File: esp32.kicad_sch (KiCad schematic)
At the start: 17 parts, among them J5 UART, J6 ToSSR, J7 USB_A, Q1 BSS138, SW1 SW_Push, SW2 SW_Push, U1 ESP32-S3-WROOM-1

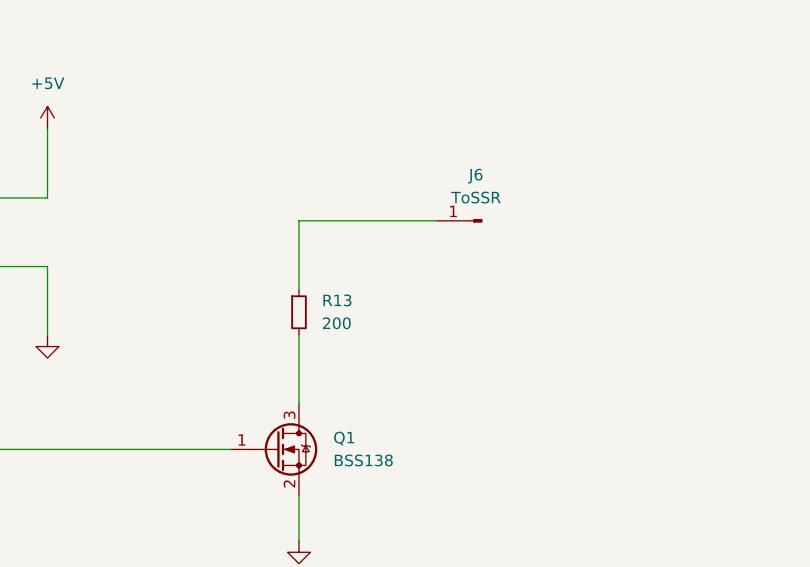
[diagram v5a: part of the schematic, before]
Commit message: fix: add connector JST to SSR device
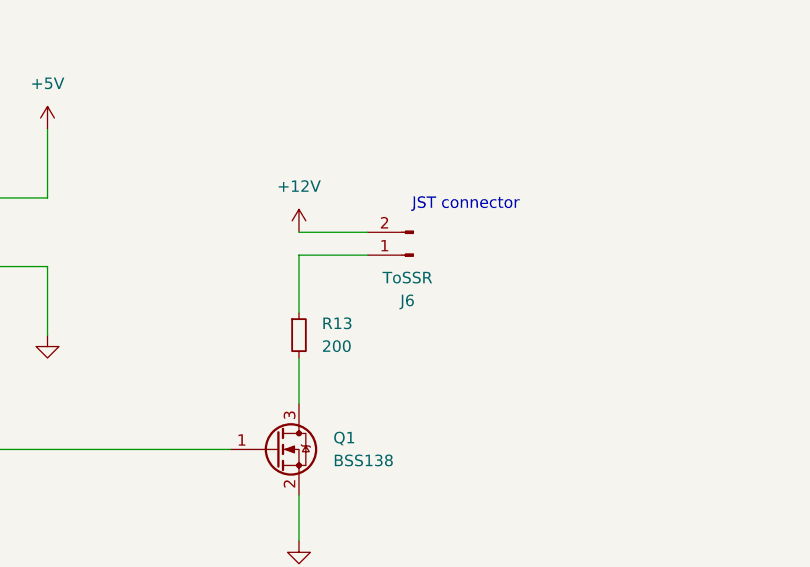
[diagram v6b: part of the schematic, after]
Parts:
- removed J6: ToSSR, Connector_PinHeader_2.54mm:PinHeader_1x01_P2.54mm_Vertical, symbol Connector:Conn_01x01_Pin
- added J6: ToSSR, symbol Connector:Conn_01x02_Pin
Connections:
- net at R13.1: now also J6.1 (Pin_1)
- new net +12V: J6.2 (Pin_2)
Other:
- note added: "JST connector"
- moved on the sheet: R13
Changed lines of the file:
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@@
 	(generator_version "9.0")
 	(paper "A4")
+	(text "JST connector"
+		(exclude_from_sim no)
+		(at 188.722 64.262 0)
+		(effects
+			(font
+				(size 1.27 1.27)
+			)
+		)
+	)
 	(junction
 		(at 92.71 44.45)
@@
 	(wire
 		(pts
-			(xy 170.18 78.74) (xy 170.18 86.36)
+			(xy 170.18 81.28) (xy 170.18 86.36)
 		)
 		(stroke
@@
 	(wire
 		(pts
-			(xy 170.18 66.04) (xy 170.18 73.66)
+			(xy 170.18 69.85) (xy 170.18 76.2)
 		)
 		(stroke
@@
 	(wire
 		(pts
+			(xy 170.18 67.31) (xy 177.8 67.31)
+		)
+		(stroke
+			(width 0)
+			(type default)
+		)
+	)
+	(wire
+		(pts
 			(xy 107.95 91.44) (xy 162.56 91.44)
 		)
@@
 	(wire
 		(pts
-			(xy 185.42 66.04) (xy 170.18 66.04)
-		)
-		(stroke
-			(width 0)
-			(type default)
-		)
-	)
-	(wire
-		(pts
 			(xy 142.24 55.88) (xy 142.24 63.5)
+		)
+		(stroke
+			(width 0)
+			(type default)
+		)
+	)
+	(wire
+		(pts
+			(xy 170.18 69.85) (xy 177.8 69.85)
 		)
 		(stroke
@@
 	(symbol
 		(lib_id "Device:R_Small")
-		(at 170.18 76.2 0)
+		(at 170.18 78.74 0)
 		(unit 1)
 		(exclude_from_sim no)
@@
 		(fields_autoplaced yes)
 		(property "Reference" "R13"
-			(at 172.72 74.93 0)
+			(at 172.72 77.47 0)
 			(effects
 				(font
@@
 		)
 		(property "Value" "200"
-			(at 172.72 77.47 0)
+			(at 172.72 80.01 0)
 			(effects
 				(font
@@
 		)
 		(property "Footprint" "Resistor_THT:R_Axial_DIN0207_L6.3mm_D2.5mm_P7.62mm_Horizontal"
-			(at 170.18 76.2 0)
+			(at 170.18 78.74 0)
 			(effects
 				(font
@@
 		)
 		(property "Datasheet" "dispo 180 ou 220"
-			(at 170.18 76.2 0)
+			(at 170.18 78.74 0)
 			(effects
 				(font
@@
 		)
 		(property "Description" ""
-			(at 170.18 76.2 0)
+			(at 170.18 78.74 0)
 			(effects
 				(font
@@
 	)
 	(symbol
-		(lib_id "Connector:Conn_01x01_Pin")
-		(at 190.5 66.04 180)
-		(unit 1)
-		(exclude_from_sim no)
-		(in_bom yes)
-		(on_board yes)
-		(dnp no)
-		(fields_autoplaced yes)
-		(property "Reference" "J6"
-			(at 189.865 60.96 0)
-			(effects
-				(font
-					(size 1.27 1.27)
-				)
-			)
-		)
-		(property "Value" "ToSSR"
-			(at 189.865 63.5 0)
-			(effects
-				(font
-					(size 1.27 1.27)
-				)
-			)
-		)
-		(property "Footprint" "Connector_PinHeader_2.54mm:PinHeader_1x01_P2.54mm_Vertical"
-			(at 190.5 66.04 0)
-			(effects
-				(font
-					(size 1.27 1.27)
-				)
-				(hide yes)
-			)
-		)
-		(property "Datasheet" "~"
-			(at 190.5 66.04 0)
-			(effects
-				(font
-					(size 1.27 1.27)
-				)
-				(hide yes)
-			)
-		)
-		(property "Description" ""
-			(at 190.5 66.04 0)
-			(effects
-				(font
-					(size 1.27 1.27)
-				)
-				(hide yes)
-			)
-		)
-		(pin "1"
-		)
-		(instances
-			(project "pv_router"
-				(path "/08ef31dc-81c2-4bcd-8336-e62c344e451e/5b2a06a5-fb5f-4aba-bfde-32c85173e89f"
-					(reference "J6")
-					(unit 1)
-				)
-			)
-		)
-	)
-	(symbol
 		(lib_id "Device:C")
 		(at 60.96 66.04 90)
@@
 	)
 	(symbol
+		(lib_id "power:+12V")
+		(at 170.18 67.31 0)
+		(unit 1)
+		(exclude_from_sim no)
+		(in_bom yes)
+		(on_board yes)
+		(dnp no)
+		(fields_autoplaced yes)
+		(property "Reference" "#PWR020"
+			(at 170.18 71.12 0)
+			(effects
+				(font
+					(size 1.27 1.27)
+				)
+				(hide yes)
+			)
+		)
+		(property "Value" "+12V"
+			(at 170.18 62.23 0)
+			(effects
+				(font
+					(size 1.27 1.27)
+				)
+			)
+		)
+		(property "Footprint" ""
+			(at 170.18 67.31 0)
+			(effects
+				(font
+					(size 1.27 1.27)
+				)
+				(hide yes)
+			)
+		)
+		(property "Datasheet" ""
+			(at 170.18 67.31 0)
+			(effects
+				(font
+					(size 1.27 1.27)
+				)
+				(hide yes)
+			)
+		)
+		(property "Description" "Power symbol creates a global label with name \"+12V\""
+			(at 170.18 67.31 0)
+			(effects
+				(font
+					(size 1.27 1.27)
+				)
+				(hide yes)
+			)
+		)
+		(pin "1"
+		)
+		(instances
+			(project ""
+				(path "/08ef31dc-81c2-4bcd-8336-e62c344e451e/5b2a06a5-fb5f-4aba-bfde-32c85173e89f"
+					(reference "#PWR020")
+					(unit 1)
+				)
+			)
+		)
+	)
+	(symbol
 		(lib_id "Device:R")
 		(at 128.27 119.38 180)
@@
 					(unit 1)
 				)
+			)
+		)
+	)
+	(symbol
+		(lib_id "Connector:Conn_01x02_Pin")
+		(at 182.88 69.85 180)
+		(unit 1)
+		(exclude_from_sim no)
+		(in_bom yes)
+		(on_board yes)
+		(dnp no)
+		(fields_autoplaced yes)
+		(property "Reference" "J6"
+			(at 182.245 74.93 0)
+			(effects
+				(font
+					(size 1.27 1.27)
+				)
+			)
+		)
+		(property "Value" "ToSSR"
+			(at 182.245 72.39 0)
+			(effects
+				(font
+					(size 1.27 1.27)
+				)
+			)
+		)
+		(property "Footprint" ""
+			(at 182.88 69.85 0)
+			(effects
+				(font
+					(size 1.27 1.27)
+				)
+				(hide yes)
+			)
+		)
+		(property "Datasheet" "~"
+			(at 182.88 69.85 0)
+			(effects
+				(font
+					(size 1.27 1.27)
+				)
+				(hide yes)
+			)
+		)
+		(property "Description" "JST HS connector"
+			(at 182.88 69.85 0)
+			(effects
+				(font
+					(size 1.27 1.27)
+				)
+				(hide yes)
+			)
+		)
+		(pin "2"
+		)
+		(pin "1"
+		)
+		(instances
+			(project ""
+				(path "/08ef31dc-81c2-4bcd-8336-e62c344e451e/5b2a06a5-fb5f-4aba-bfde-32c85173e89f"
+					(reference "J6")
+					(unit 1)
+				)

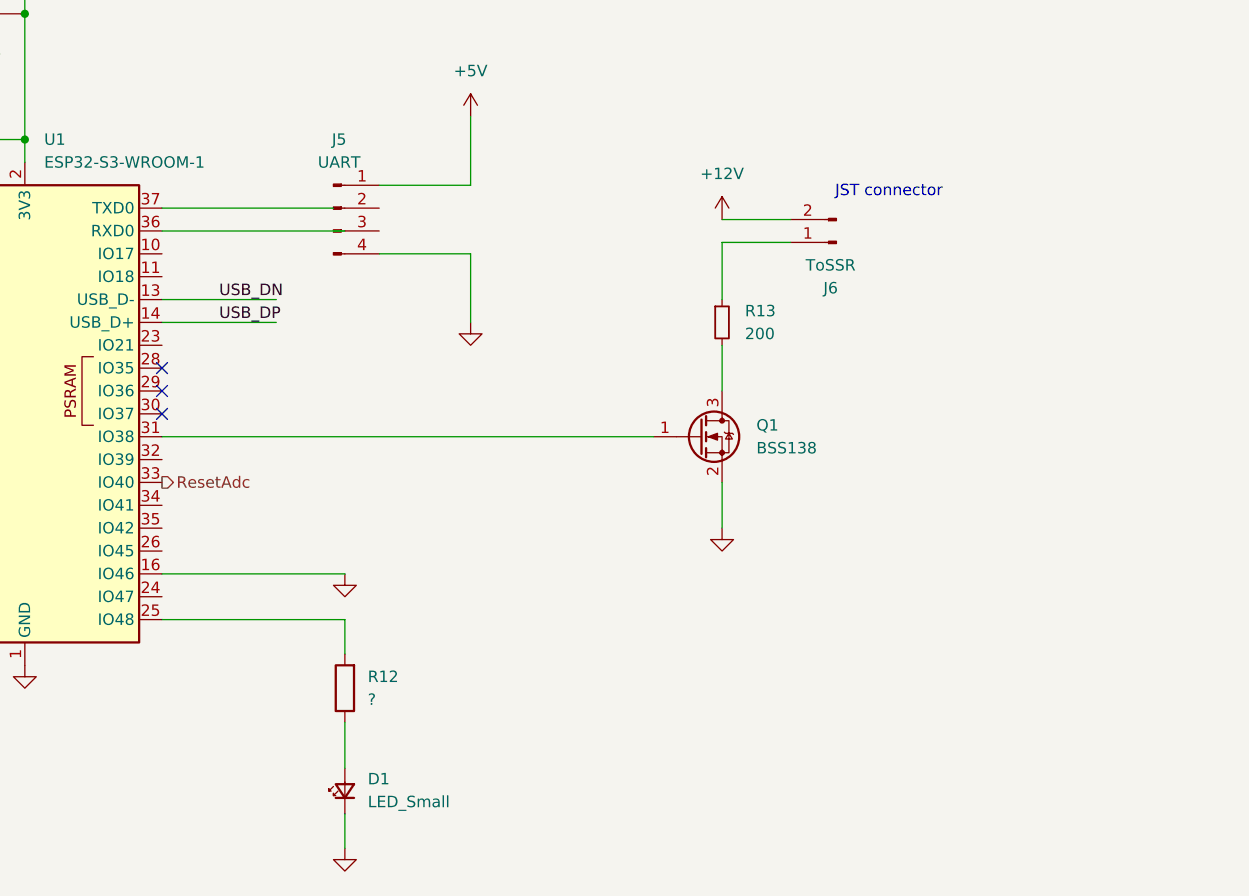
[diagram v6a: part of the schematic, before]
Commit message: feat: add led lighting when SSR is on
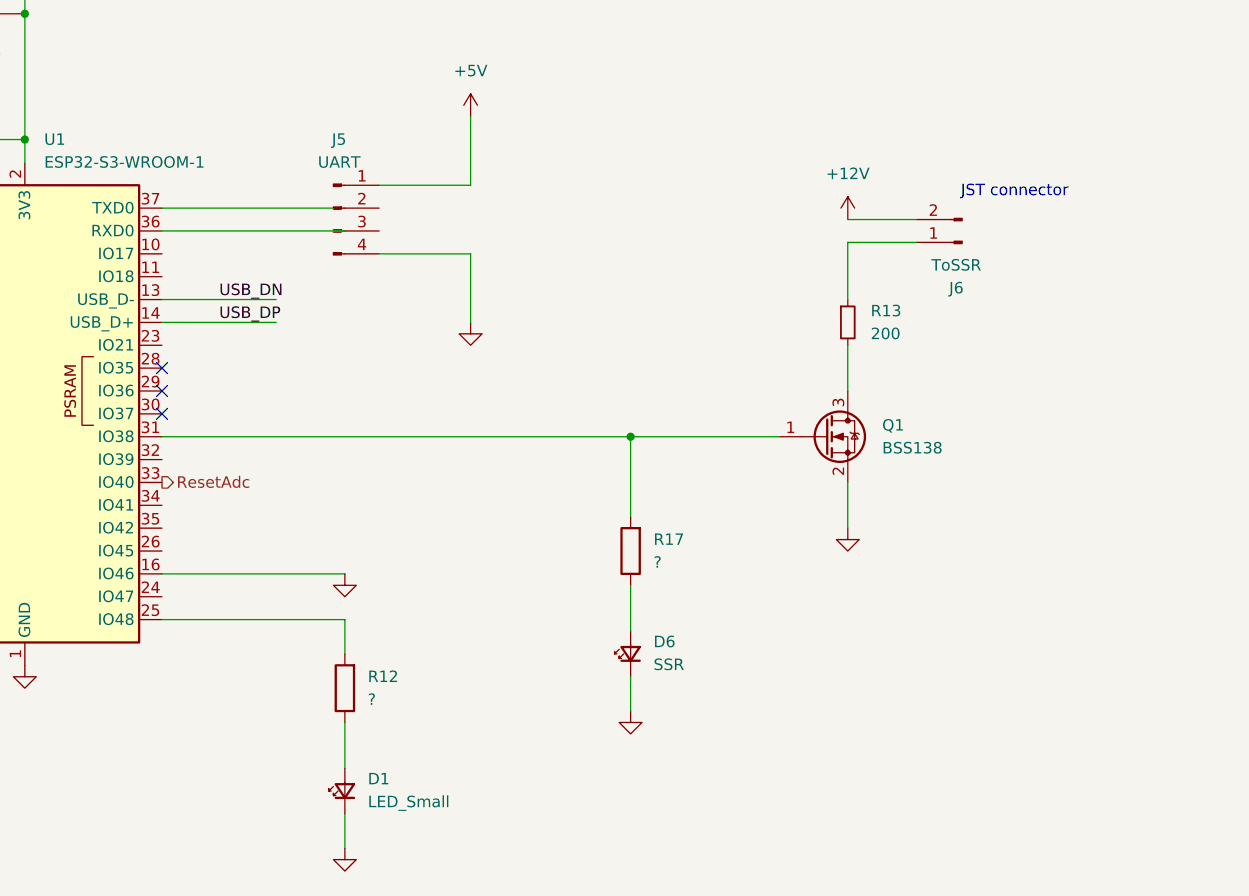
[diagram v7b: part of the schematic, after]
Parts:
- added D6: SSR, LED_SMD:LED_0805_2012Metric, symbol Device:LED_Small
- added R17: ?, Resistor_THT:R_Axial_DIN0207_L6.3mm_D2.5mm_P7.62mm_Horizontal, symbol Device:R
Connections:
- net GND: now also D6.1 (K)
- net at Q1.1 (G), U1.31 (IO38): now also R17.2
- new net: D6.2 (A), R17.1
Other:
- moved on the sheet: J6, Q1, R13
